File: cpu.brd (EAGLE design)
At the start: 72.4 x 38.1 mm, 86 parts, among them X1 ED060SC4_EINK, X10 PIIKKIRIMA-4, X2 PIIKKIRIMA-5, X3 PIIKKIRIMA-2, X4 629105136821, X5 693071010811, X6 PIIKKIRIMA-6, X7 PIIKKIRIMA-2, X8 PIIKKIRIMA-2, X9 PIIKKIRIMA-2

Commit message: HSE Crystal added
Added G1, 3.2x2.5 mm crystal. bottom.
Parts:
- added C23, C24: (no value), rcl:C0603
- added G1: XTAL_3225_SMD, OMAT_IC:X_3225
- moved R17 0.25 mm to (9.86, 16.6)
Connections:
- new net N$12: C23.2, D1.5, G1.1
- new net N$14: C24.2, D1.6, G1.3
- net GND: now also C23.1, C24.1
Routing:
- net N$12: track 0.00 -> 11.3 mm, vias 0 -> 1
- net LED3: track 29.9 -> 36.5 mm
- net LED4: track 27.1 -> 32.6 mm
- net N$14: track 0.00 -> 4.87 mm, vias 0 -> 1
- net GND: vias 110 -> 113

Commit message: Bypass, tuning
One 0805 bulk bypass added.
GND fills fixed close G1
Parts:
- added C25: (no value), rcl:C0805
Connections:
- net +3V3: now also C25.1
- net GND: now also C25.2
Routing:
- net +3V3: track 184.0 -> 185.1 mm
- net GND: vias 113 -> 120
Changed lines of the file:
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@@
 <layer number="19" name="Unrouted" color="12" fill="1" visible="yes" active="yes"/>
 <layer number="20" name="Dimension" color="15" fill="1" visible="yes" active="yes"/>
-<layer number="21" name="tPlace" color="7" fill="1" visible="no" active="yes"/>
-<layer number="22" name="bPlace" color="7" fill="1" visible="yes" active="yes"/>
-<layer number="23" name="tOrigins" color="15" fill="1" visible="no" active="yes"/>
-<layer number="24" name="bOrigins" color="15" fill="1" visible="yes" active="yes"/>
-<layer number="25" name="tNames" color="7" fill="1" visible="no" active="yes"/>
-<layer number="26" name="bNames" color="7" fill="1" visible="yes" active="yes"/>
+<layer number="21" name="tPlace" color="7" fill="1" visible="yes" active="yes"/>
+<layer number="22" name="bPlace" color="7" fill="1" visible="no" active="yes"/>
+<layer number="23" name="tOrigins" color="15" fill="1" visible="yes" active="yes"/>
+<layer number="24" name="bOrigins" color="15" fill="1" visible="no" active="yes"/>
+<layer number="25" name="tNames" color="7" fill="1" visible="yes" active="yes"/>
+<layer number="26" name="bNames" color="7" fill="1" visible="no" active="yes"/>
 <layer number="27" name="tValues" color="7" fill="1" visible="no" active="yes"/>
 <layer number="28" name="bValues" color="7" fill="1" visible="no" active="yes"/>
@@
 <attribute name="VALUE" x="58.928" y="21.9075" size="1.27" layer="28" rot="MR180"/>
 </element>
+<element name="C25" library="rcl" package="C0805" value="" x="68.3895" y="7.9375" smashed="yes" rot="R270">
+<attribute name="NAME" x="67.31" y="5.2705" size="0.8128" layer="25"/>
+<attribute name="VALUE" x="65.8495" y="9.2075" size="1.27" layer="27" rot="R270"/>
+</element>
 </elements>
 <signals>
@@
 <via x="55.5625" y="25.908" extent="1-16" drill="0.3302"/>
 <via x="40.513" y="25.4" extent="1-16" drill="0.3302"/>
+<via x="61.2775" y="20.828" extent="1-16" drill="0.3302"/>
+<via x="57.2135" y="22.733" extent="1-16" drill="0.3302"/>
+<via x="56.4515" y="21.2725" extent="1-16" drill="0.3302"/>
+<via x="51.435" y="30.734" extent="1-16" drill="0.3302"/>
+<via x="58.2295" y="30.988" extent="1-16" drill="0.3302"/>
+<via x="68.707" y="23.3045" extent="1-16" drill="0.3302"/>
+<via x="68.58" y="11.43" extent="1-16" drill="0.3302"/>
+<contactref element="C25" pad="2"/>
 </signal>
 <signal name="N$3">
@@
 <wire x1="56.642" y1="10.2235" x2="58.293" y2="10.2235" width="0.1524" layer="1"/>
 <wire x1="58.293" y1="10.2235" x2="58.6105" y2="10.2235" width="0.1524" layer="1"/>
-<wire x1="65.2653" y1="12.2633" x2="62.3721" y2="12.2633" width="0.1524" layer="1"/>
+<wire x1="65.2653" y1="12.2633" x2="62.3721" y2="12.2633" width="0.254" layer="1"/>
 <wire x1="62.3721" y1="12.2633" x2="62.3062" y2="12.3292" width="0.1524" layer="1"/>
 <wire x1="60.0075" y1="9.5885" x2="60.0075" y2="10.287" width="0.1524" layer="1"/>
-<wire x1="60.0075" y1="10.287" x2="60.0075" y2="10.9855" width="0.1524" layer="1"/>
-<wire x1="60.0075" y1="10.9855" x2="61.341" y2="12.319" width="0.1524" layer="1"/>
-<wire x1="61.341" y1="12.319" x2="62.296" y2="12.319" width="0.1524" layer="1"/>
+<wire x1="60.0075" y1="10.287" x2="60.0075" y2="10.9855" width="0.254" layer="1"/>
+<wire x1="60.0075" y1="10.9855" x2="61.341" y2="12.319" width="0.254" layer="1"/>
+<wire x1="61.341" y1="12.319" x2="62.296" y2="12.319" width="0.254" layer="1"/>
 <wire x1="62.296" y1="12.319" x2="62.3062" y2="12.3292" width="0.1524" layer="1"/>
 <wire x1="58.6105" y1="10.2235" x2="58.674" y2="10.287" width="0.1524" layer="1"/>
@@
 <wire x1="42.9895" y1="17.272" x2="42.1005" y2="17.272" width="0.508" layer="1"/>
 <wire x1="42.1005" y1="17.272" x2="39.9415" y2="15.113" width="0.508" layer="1"/>
-<wire x1="66.2305" y1="10.033" x2="69.342" y2="10.033" width="0.508" layer="1"/>
+<wire x1="66.2305" y1="10.033" x2="68.3895" y2="10.033" width="0.508" layer="1"/>
+<wire x1="68.3895" y1="10.033" x2="69.342" y2="10.033" width="0.508" layer="1"/>
 <wire x1="69.342" y1="10.033" x2="70.9295" y2="11.6205" width="0.508" layer="1"/>
 <wire x1="70.9295" y1="11.6205" x2="70.9295" y2="23.4315" width="0.508" layer="1"/>
@@
 <wire x1="56.134" y1="31.8135" x2="56.134" y2="31.8128" width="0.1524" layer="1"/>
 <wire x1="56.134" y1="31.8128" x2="56.0832" y2="31.762" width="0.1524" layer="1"/>
+<contactref element="C25" pad="1"/>
+<wire x1="68.3895" y1="8.8875" x2="68.3895" y2="10.033" width="0.508" layer="1"/>
 </signal>
 <signal name="VSSA">
@@
 <wire x1="31.9394" y1="34.1746" x2="31.9659" y2="34.2011" width="0.254" layer="1"/>
 <wire x1="58.9915" y1="22.0218" x2="56.5658" y2="22.0218" width="0.1524" layer="1"/>
-<wire x1="56.5658" y1="22.0218" x2="56.261" y2="21.717" width="0.1524" layer="1"/>
-<wire x1="56.261" y1="21.717" x2="55.372" y2="21.717" width="0.1524" layer="1"/>
-<wire x1="55.372" y1="21.717" x2="54.991" y2="21.336" width="0.1524" layer="1"/>
+<wire x1="56.5658" y1="22.0218" x2="56.388" y2="21.844" width="0.1524" layer="1"/>
+<wire x1="56.388" y1="21.844" x2="55.499" y2="21.844" width="0.1524" layer="1"/>
+<wire x1="55.499" y1="21.844" x2="54.991" y2="21.336" width="0.1524" layer="1"/>
 <wire x1="54.991" y1="21.336" x2="51.308" y2="21.336" width="0.1524" layer="1"/>
 <wire x1="51.308" y1="21.336" x2="50.419" y2="20.447" width="0.1524" layer="1"/>

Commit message: Power control signals added
DCDC Converter enables (all three) were missing from schematic.
Processor grounds connected too.
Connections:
- removed net VSSA: D1.12
- removed net VSS_1: D1.31
- removed net VSS_2: D1.47
- removed net VSS_3: D1.63
- removed net VSS_4: D1.18
- net GND: now also D1.12, D1.18, D1.31, D1.47, D1.63
- net VEINK_CTRLN: now also D1.54
- net VNEG_CTRLN: now also D1.38
- net VPOS_CTRLN: now also D1.37
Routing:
- net VEINK_CTRLN: track 1.72 -> 74.2 mm, vias 0 -> 4
- net VNEG_CTRLN: track 10.4 -> 65.5 mm, vias 2 -> 9
- net VPOS_CTRLN: track 19.7 -> 74.5 mm, vias 2 -> 9
- net GND: track 92.9 -> 91.4 mm, vias 120 -> 141
- net EINKD2: track 37.3 -> 38.5 mm
- net N$20: track 63.2 -> 62.4 mm
- net BOOT0: track 56.0 -> 55.3 mm
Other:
- board text added: "+"

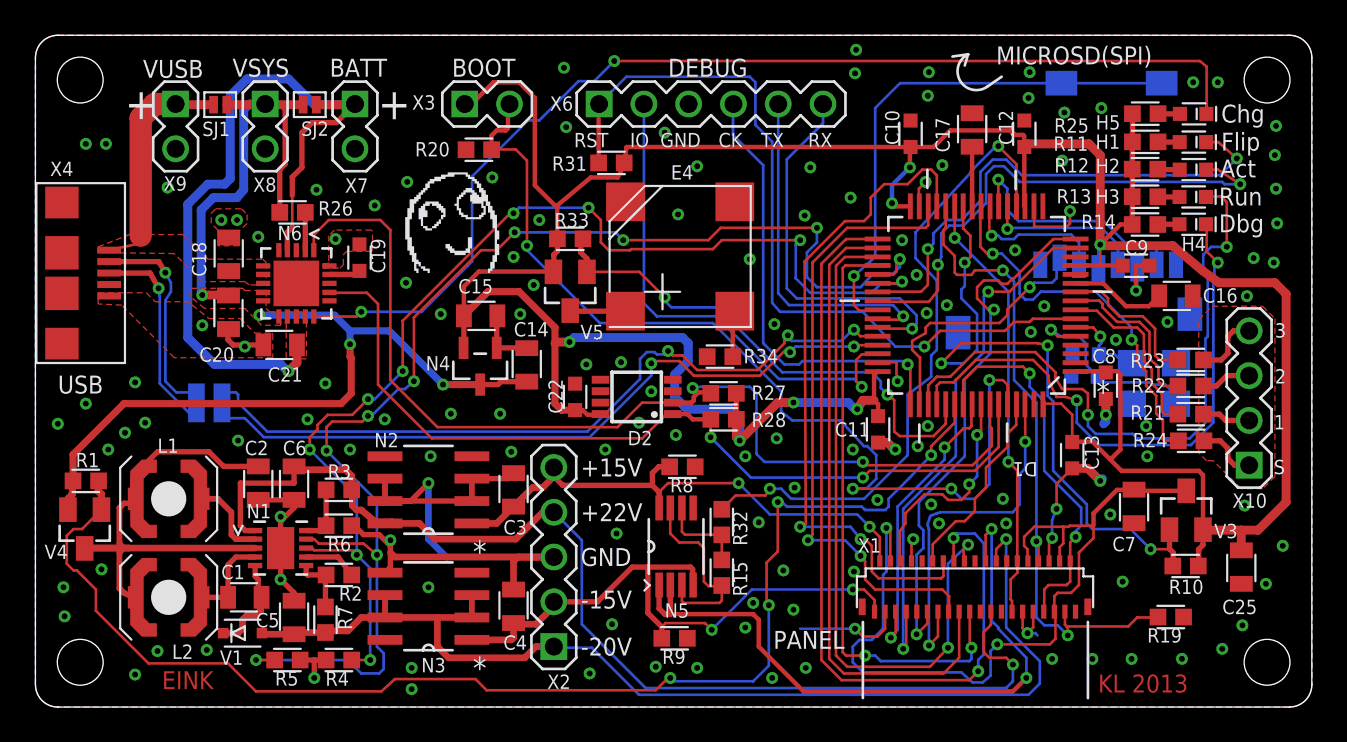
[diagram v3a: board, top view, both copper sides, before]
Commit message: Final - ready to order
Part values added
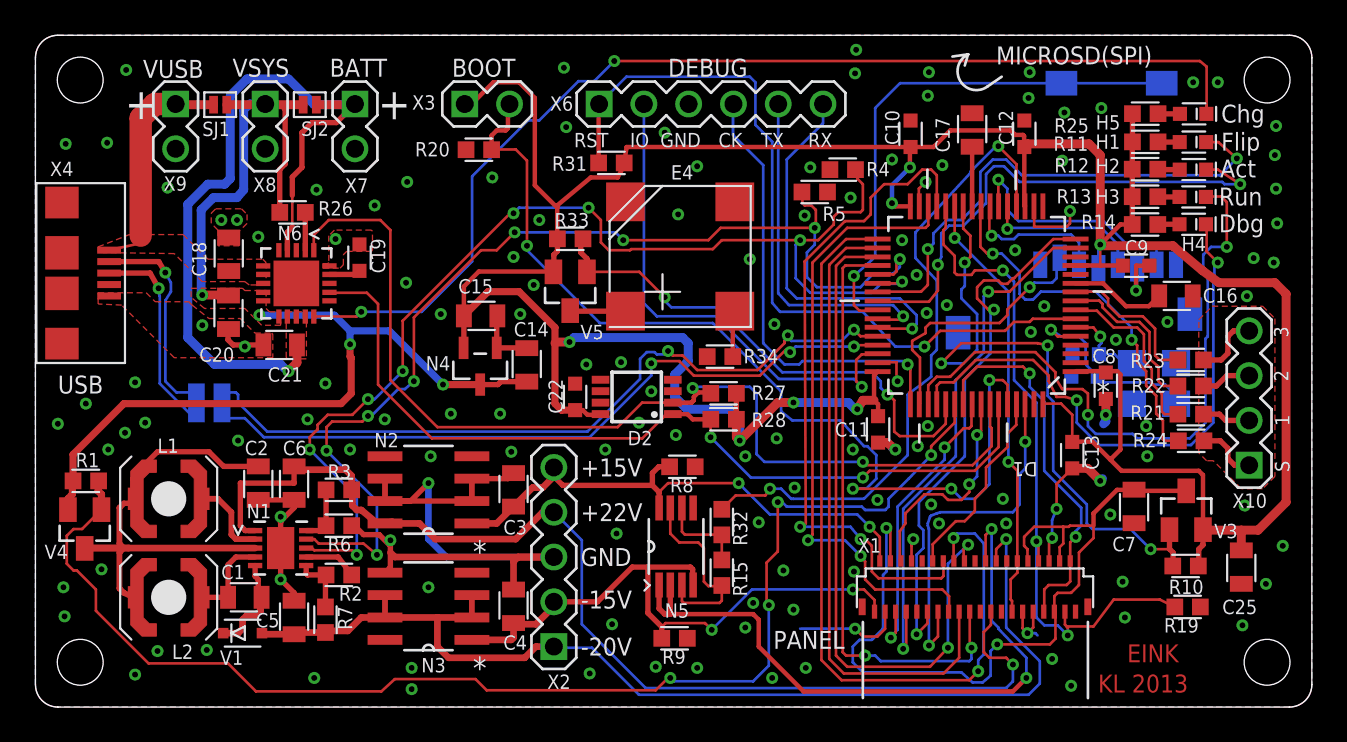
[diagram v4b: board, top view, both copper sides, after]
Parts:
- removed U$2: DAFUG, dafug:DAFUG
- added U$3: (no value), dafug:DAFUG
- C1, C14, C7: value (none) -> 1u 50V
- C10, C11, C12, C13, C19, C22, C8, C9: value (none) -> 100n
- C15, C18, C20, C21, C25: value (none) -> 10u 10V
- C2, C3, C4, C5, C6: value (none) -> 4u7 50V
- C23, C24: value (none) -> 12p
- H1, H2, H3: value (none) -> GRN
- H4, H5: value (none) -> YEL
- N5: value MAX412CPAMSOP -> LM358
- R1, R10, R19, R2, R20, R21, R22, R23, R24, R26, R31, R33, R4, R5, R6, R8, R9: value (none) -> 10k
- R11, R12, R13, R14, R25: value (none) -> 511R
- R15, R32: value 5k11 -> 10k
- R27, R28: value (none) -> 2k15
- R3: value (none) -> 165k
- R34: value (none) -> 22R
- R7: value (none) -> 160k
- V3, V4, V5: value DMG2307LSOT23 -> FDV304
- moved R5 40.0 mm to (44.2, 29.2)
- moved R4 39.9 mm to (45.8, 30.5)
- moved R19 1.11 mm to (65.3, 5.68)
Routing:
- net VPOS_CTRLN: track 74.5 -> 61.6 mm, vias 9 -> 8
- net GND: track 91.4 -> 88.9 mm
- net SPV/BOOT1: track 37.6 -> 39.2 mm
- net VNEG_CTRLN: track 65.5 -> 65.7 mm, vias 9 -> 8
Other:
- board text added: "eInk Display Controller V1.0 KL 13.9.2013"
- board text removed: "eInk Display Controler V1.0 KL 12.9.2013"

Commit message: KIMDLE logo
Logo added - saying KIMDLE on bottom
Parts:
- added U$1: (no value), dafug:KIMDLE
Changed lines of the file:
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@@
 <setting verticaltext="up"/>
 </settings>
-<grid distance="0.0025" unitdist="inch" unit="inch" style="lines" multiple="1" display="no" altdistance="0.025" altunitdist="inch" altunit="inch"/>
+<grid distance="0.001667" unitdist="inch" unit="inch" style="lines" multiple="1" display="yes" altdistance="0.025" altunitdist="inch" altunit="inch"/>
 <layers>
-<layer number="1" name="Top" color="2" fill="1" visible="yes" active="yes"/>
+<layer number="1" name="Top" color="2" fill="1" visible="no" active="yes"/>
 <layer number="2" name="Route2" color="1" fill="3" visible="no" active="no"/>
 <layer number="3" name="Route3" color="4" fill="3" visible="no" active="no"/>
 <layer number="14" name="Route14" color="1" fill="6" visible="no" active="no"/>
 <layer number="15" name="Route15" color="4" fill="6" visible="no" active="no"/>
-<layer number="16" name="Bottom" color="1" fill="1" visible="no" active="yes"/>
+<layer number="16" name="Bottom" color="1" fill="1" visible="yes" active="yes"/>
 <layer number="17" name="Pads" color="13" fill="1" visible="yes" active="yes"/>
 <layer number="18" name="Vias" color="2" fill="1" visible="yes" active="yes"/>
 <layer number="19" name="Unrouted" color="12" fill="1" visible="no" active="yes"/>
-<layer number="20" name="Dimension" color="15" fill="1" visible="yes" active="yes"/>
-<layer number="21" name="tPlace" color="7" fill="1" visible="yes" active="yes"/>
-<layer number="22" name="bPlace" color="7" fill="1" visible="no" active="yes"/>
-<layer number="23" name="tOrigins" color="15" fill="1" visible="yes" active="yes"/>
+<layer number="20" name="Dimension" color="15" fill="1" visible="no" active="yes"/>
+<layer number="21" name="tPlace" color="7" fill="1" visible="no" active="yes"/>
+<layer number="22" name="bPlace" color="7" fill="1" visible="yes" active="yes"/>
+<layer number="23" name="tOrigins" color="15" fill="1" visible="no" active="yes"/>
 <layer number="24" name="bOrigins" color="15" fill="1" visible="no" active="yes"/>
-<layer number="25" name="tNames" color="7" fill="1" visible="yes" active="yes"/>
+<layer number="25" name="tNames" color="7" fill="1" visible="no" active="yes"/>
 <layer number="26" name="bNames" color="7" fill="1" visible="no" active="yes"/>
 <layer number="27" name="tValues" color="7" fill="1" visible="no" active="yes"/>
@@
 <layer number="151" name="HeatSink" color="7" fill="1" visible="no" active="yes"/>
 <layer number="199" name="Contour" color="7" fill="1" visible="no" active="yes"/>
-<layer number="200" name="200bmp" color="1" fill="10" visible="no" active="yes"/>
+<layer number="200" name="200bmp" color="1" fill="10" visible="yes" active="yes"/>
 <layer number="201" name="201bmp" color="2" fill="10" visible="no" active="yes"/>
 <layer number="202" name="202bmp" color="3" fill="10" visible="no" active="yes"/>
@@
 </element>
 <element name="U$3" library="dafug" package="DAFUG" value="" x="9.0805" y="9.906" rot="MR0"/>
+<element name="U$1" library="dafug" package="KIMDLE" value="" x="51.064209375" y="16.513303125" rot="MR0"/>
 </elements>
 <signals>
@@
 </signal>
 </signals>
-<errors>
-</errors>
 </board>
 </drawing>
